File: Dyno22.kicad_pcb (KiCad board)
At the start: 2 copper layers, 160 x 110 mm, 44 parts, among them J1 Pwr Input, J2 Display, J3 Pwr Output, J4 BPM & Sensors, J7 UART, U1 TS2937CW50, U2 LM324, U3 74HC4052

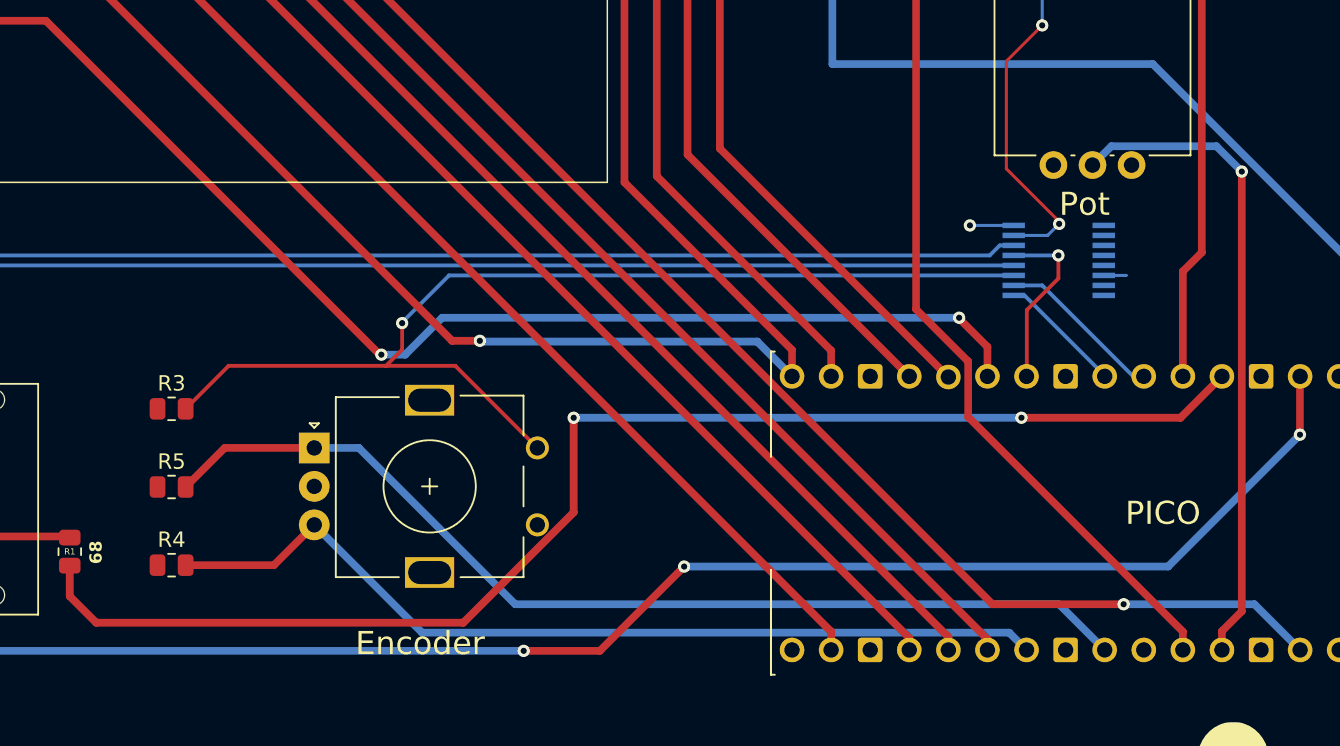
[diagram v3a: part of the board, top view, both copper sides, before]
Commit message: Fixed traces DRC
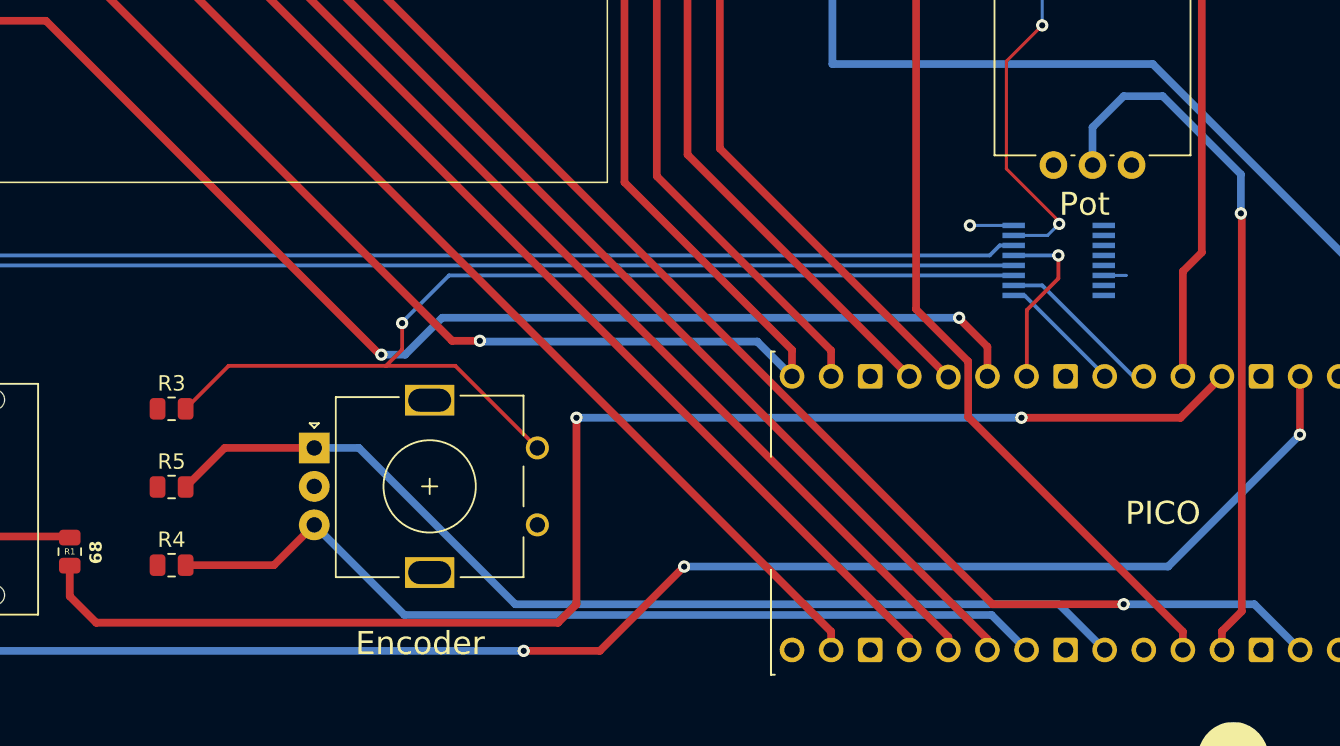
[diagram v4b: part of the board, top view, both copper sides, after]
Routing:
- net /BPM_CTRL_IN: track 42.5 -> 46.5 mm
- net /LED_SELECT: track 87.6 -> 91.1 mm
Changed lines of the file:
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@@
   (segment (start 195.93 119.47) (end 204.5 110.9) (width 0.5) (layer "B.Cu") (net 8))
   (segment (start 164.48 119.47) (end 195.93 119.47) (width 0.5) (layer "B.Cu") (net 8))
+  (segment (start 186.4 109.8) (end 196.74 109.8) (width 0.508) (layer "F.Cu") (net 9))
+  (segment (start 157.48 109.8) (end 157.48 121.92) (width 0.508) (layer "F.Cu") (net 9))
+  (segment (start 124.55 121.4) (end 124.55 119.625) (width 0.508) (layer "F.Cu") (net 9))
   (segment (start 126.27 123.12) (end 124.55 121.4) (width 0.508) (layer "F.Cu") (net 9))
-  (segment (start 186.4 109.8) (end 196.74 109.8) (width 0.508) (layer "F.Cu") (net 9))
-  (segment (start 150.13 123.12) (end 126.27 123.12) (width 0.508) (layer "F.Cu") (net 9))
-  (segment (start 157.3 109.8) (end 157.3 115.95) (width 0.508) (layer "F.Cu") (net 9))
-  (segment (start 157.3 115.95) (end 150.13 123.12) (width 0.508) (layer "F.Cu") (net 9))
+  (segment (start 157.48 121.92) (end 156.28 123.12) (width 0.508) (layer "F.Cu") (net 9))
+  (segment (start 156.28 123.12) (end 126.27 123.12) (width 0.508) (layer "F.Cu") (net 9))
   (segment (start 196.74 109.8) (end 199.43 107.11) (width 0.508) (layer "F.Cu") (net 9))
-  (segment (start 124.55 121.4) (end 124.55 119.625) (width 0.508) (layer "F.Cu") (net 9))
   (via (at 186.4 109.8) (size 0.8) (drill 0.4) (layers "F.Cu" "B.Cu") (net 9))
-  (via (at 157.3 109.8) (size 0.8) (drill 0.4) (layers "F.Cu" "B.Cu") (net 9))
-  (segment (start 186.4 109.8) (end 157.3 109.8) (width 0.508) (layer "B.Cu") (net 9))
+  (via (at 157.48 109.8) (size 0.8) (drill 0.4) (layers "F.Cu" "B.Cu") (net 9))
+  (segment (start 186.4 109.8) (end 157.48 109.8) (width 0.508) (layer "B.Cu") (net 9))
   (segment (start 196.89 100.29) (end 196.89 107.11) (width 0.5) (layer "F.Cu") (net 10))
   (segment (start 198.12 99.06) (end 198.12 74.5725) (width 0.5) (layer "F.Cu") (net 10))
@@
   (segment (start 177.9875 52.3625) (end 177.95 52.4) (width 0.5) (layer "F.Cu") (net 22))
   (segment (start 196.89 123.698) (end 196.89 124.89) (width 0.5) (layer "F.Cu") (net 22))
-  (segment (start 200.72 93.8) (end 200.72 122.38) (width 0.5) (layer "F.Cu") (net 23))
+  (segment (start 200.66 96.52) (end 200.72 96.58) (width 0.5) (layer "F.Cu") (net 23))
+  (segment (start 200.72 96.58) (end 200.72 122.38) (width 0.5) (layer "F.Cu") (net 23))
   (segment (start 199.43 123.67) (end 199.43 124.89) (width 0.5) (layer "F.Cu") (net 23))
   (segment (start 200.72 122.38) (end 199.43 123.67) (width 0.5) (layer "F.Cu") (net 23))
-  (via (at 200.72 93.8) (size 0.8) (drill 0.4) (layers "F.Cu" "B.Cu") (net 23))
-  (segment (start 199.0739 92.1539) (end 200.72 93.8) (width 0.5) (layer "B.Cu") (net 23))
-  (segment (start 192.2423 92.1539) (end 199.0739 92.1539) (width 0.5) (layer "B.Cu") (net 23))
-  (segment (start 191.0173 93.3789) (end 192.2423 92.1539) (width 0.5) (layer "B.Cu") (net 23))
+  (via (at 200.66 96.52) (size 0.8) (drill 0.4) (layers "F.Cu" "B.Cu") (net 23))
+  (segment (start 191.0173 93.3789) (end 191.0173 90.9227) (width 0.5) (layer "B.Cu") (net 23))
+  (segment (start 193.04 88.9) (end 195.58 88.9) (width 0.5) (layer "B.Cu") (net 23))
+  (segment (start 195.58 88.9) (end 200.66 93.98) (width 0.5) (layer "B.Cu") (net 23))
+  (segment (start 200.66 93.98) (end 200.66 96.52) (width 0.5) (layer "B.Cu") (net 23))
+  (segment (start 191.0173 90.9227) (end 193.04 88.9) (width 0.5) (layer "B.Cu") (net 23))
   (segment (start 137.82 119.38) (end 140.44 116.76) (width 0.5) (layer "F.Cu") (net 25))
   (segment (start 132.08 119.38) (end 137.82 119.38) (width 0.5) (layer "F.Cu") (net 25))
-  (segment (start 147.445 123.765) (end 185.605 123.765) (width 0.5) (layer "B.Cu") (net 25))
-  (segment (start 185.605 123.765) (end 186.73 124.89) (width 0.5) (layer "B.Cu") (net 25))
-  (segment (start 140.44 116.76) (end 147.445 123.765) (width 0.5) (layer "B.Cu") (net 25))
+  (segment (start 186.73 124.89) (end 184.46 122.62) (width 0.5) (layer "B.Cu") (net 25))
+  (segment (start 184.46 122.62) (end 146.3 122.62) (width 0.5) (layer "B.Cu") (net 25))
+  (segment (start 146.3 122.62) (end 140.44 116.76) (width 0.5) (layer "B.Cu") (net 25))
   (segment (start 221.2 72.85) (end 221.2 112.45) (width 0.5) (layer "F.Cu") (net 28))
   (segment (start 214.85 66.5) (end 221.2 72.85) (width 0.5) (layer "F.Cu") (net 28))

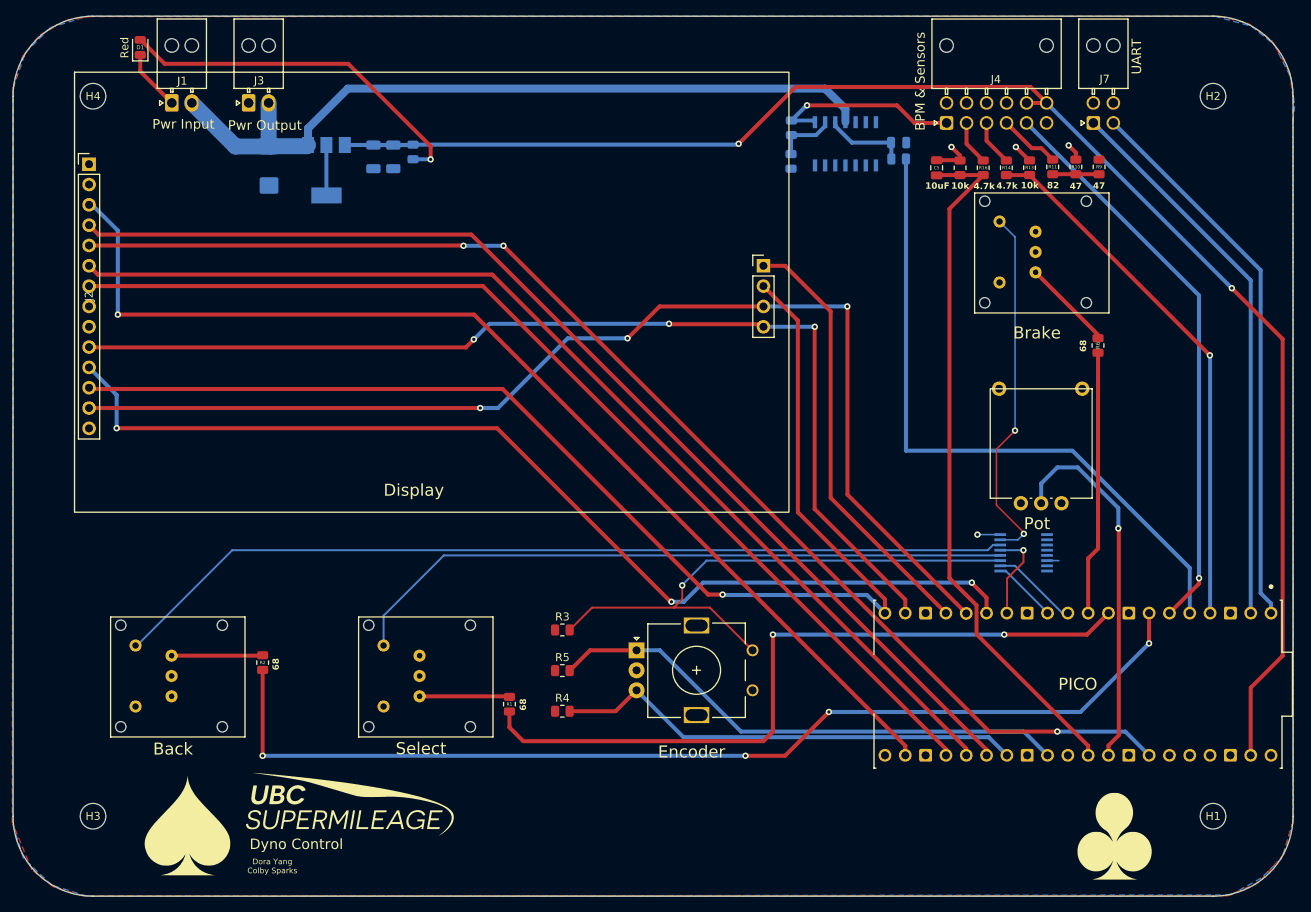
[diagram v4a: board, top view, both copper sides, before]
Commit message: moving traces for the pot
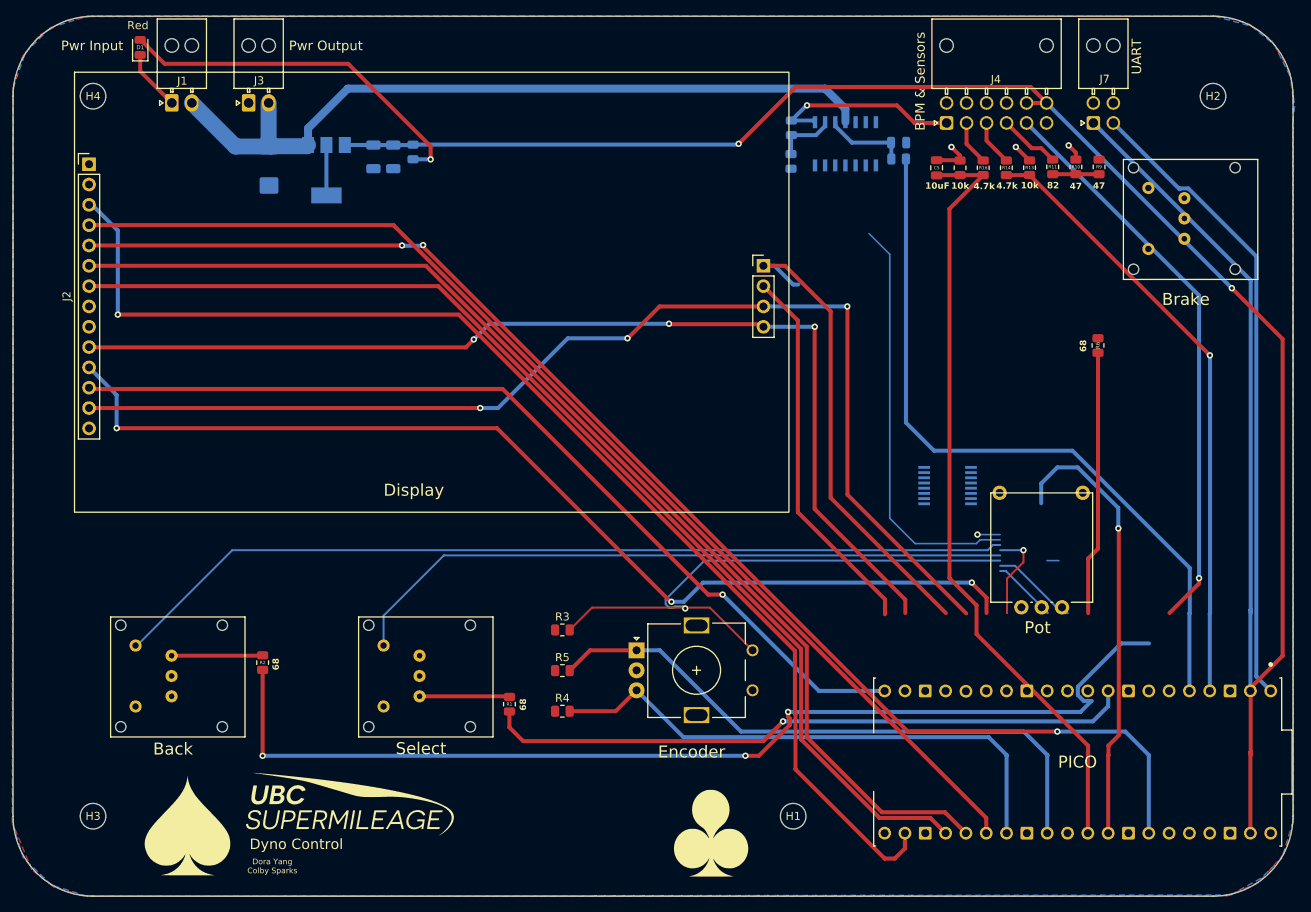
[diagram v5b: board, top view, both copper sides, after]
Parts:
- moved H1 52.5 mm to (160.0, 132.5)
- moved G*** 50.4 mm to (149.9, 134.6)
- moved S3 19.1 mm to (201.3, 50.4)
- moved RV1 13.0 mm to (184.7, 105.7)
- moved U3 12.7 mm to (179.3, 91.2)
- moved A1 9.73 mm to (195.6, 125.7)
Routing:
- net /BPM_CTRL_IN: track 46.5 -> 64.4 mm
- net /LCD_CS: track 136.6 -> 152.2 mm
- net Net-(S3-L1_Y): track 11.5 -> 0.43 mm
- net /DEMUX_S0: track 10.9 -> 0.00 mm
- net Earth: track 25.2 -> 36.1 mm
- net /UART_TX: track 69.4 -> 79.9 mm
- net +5V: track 189.5 -> 199.7 mm
- net /UART_RX: track 69.4 -> 79.6 mm
- net /FORCE_IN: track 87.3 -> 97.5 mm
- net /SCLK_0: track 131.9 -> 142.0 mm
- net /MOSI_0: track 135.5 -> 145.6 mm
- net /LED_SELECT: track 91.1 -> 81.0 mm, vias 2 -> 1
- net /LCD_DC: track 158.9 -> 168.9 mm
- net /ROT_EN_B: track 59.1 -> 68.8 mm
- net /ROT_EN_A: track 66.2 -> 76.0 mm
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
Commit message: schematic changes v2
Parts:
- removed Encoder: RotaryEncoder_Switch, Rotary_Encoder:RotaryEncoder_Alps_EC11E_Vertical_H20mm
- removed J1: Pwr Input, Connector_Molex:Molex_Nano-Fit_105313-xx02_1x02_P2.50mm_Horizontal
- added D2: LED, LED_SMD:LED_0603_1608Metric, F.Cu at (42.0, 39.6)
- added Encoder1: RotaryEncoder_Switch, Rotary_Encoder:RotaryEncoder_Alps_EC11E_Vertical_H20mm, F.Cu at (140.2, 111.8)
- added F1: Fuse 4.5A, Fuse:Fuse_1206_3216Metric, F.Cu at (42.7, 36.6)
- added J5: Pwr Input, Connector_Molex:Molex_Nano-Fit_105313-xx02_1x02_P2.50mm_Horizontal, F.Cu at (82.6, 27.5)
- added R18: 2.2k, Resistor_SMD:R_0402_1005Metric, F.Cu at (41.4, 41.9)
- added SW1: SW_DPST_x2, Button_Switch_SMD:Nidec_Copal_SH-7040B, F.Cu at (42.1, 48.3)
- added TP4: GND_TestPoint, TestPoint:TestPoint_Pad_4.0x4.0mm, F.Cu at (43.0, 32.0)
